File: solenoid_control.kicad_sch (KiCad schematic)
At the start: 37 parts, among them Q1 2N7002, Q10 DMG3406L, Q11 DMP3068L, Q12 DMG3406L, Q13 2N7002, Q14 DMP3068L, Q15 DMG3406L, Q16 DMP3068L, Q17 DMG3406L, Q19 2N7002, Q2 2N7002, Q3 DMP3068L, Q4 DMG3406L, Q5 DMP3068L, Q6 DMG3406L, Q7 2N7002, Q8 2N7002, Q9 DMP3068L

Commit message: Added connector for temperature sensor. Started to route board.
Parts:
- D14: value (none) -> BAT54S; footprint (none) -> Package_TO_SOT_SMD:SOT-23
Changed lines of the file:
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@@
       (effects (font (size 1.27 1.27)) (justify left))
     )
-    (property "Value" "" (id 1) (at 173.99 39.3699 90)
+    (property "Value" "BAT54S" (id 1) (at 173.99 39.3699 90)
       (effects (font (size 1.27 1.27)) (justify left))
     )
-    (property "Footprint" "" (id 2) (at 174.625 36.195 0)
+    (property "Footprint" "Package_TO_SOT_SMD:SOT-23" (id 2) (at 174.625 36.195 0)
       (effects (font (size 1.27 1.27)) (justify left) hide)
     )

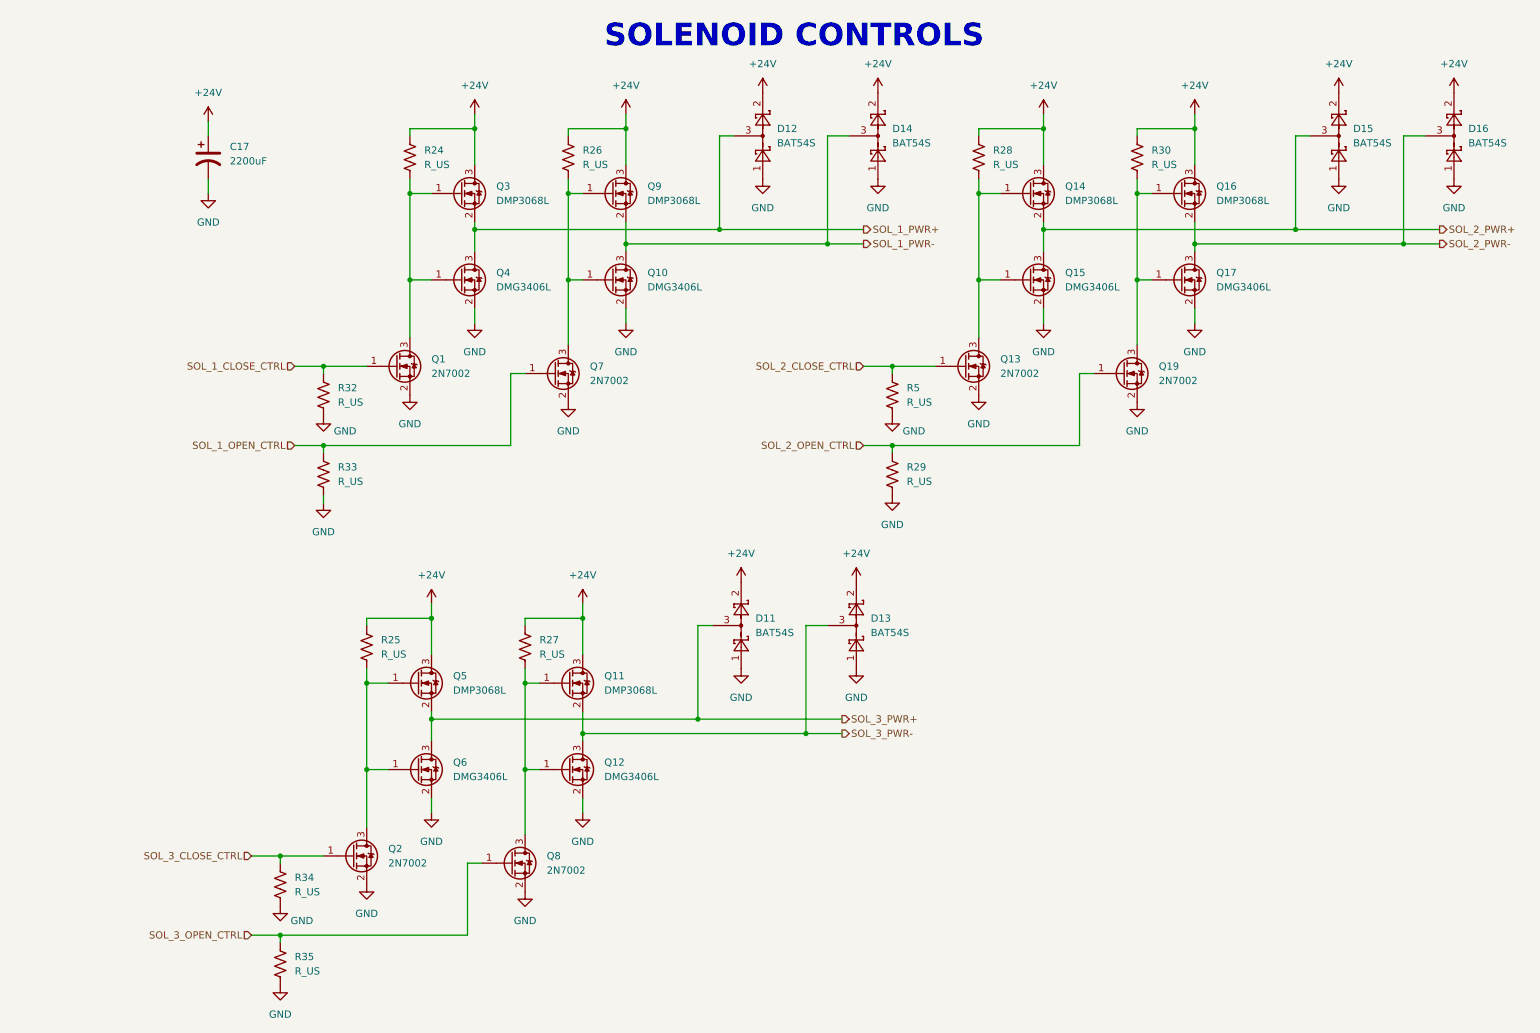
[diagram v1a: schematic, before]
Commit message: Added clamping diode for 24V net.
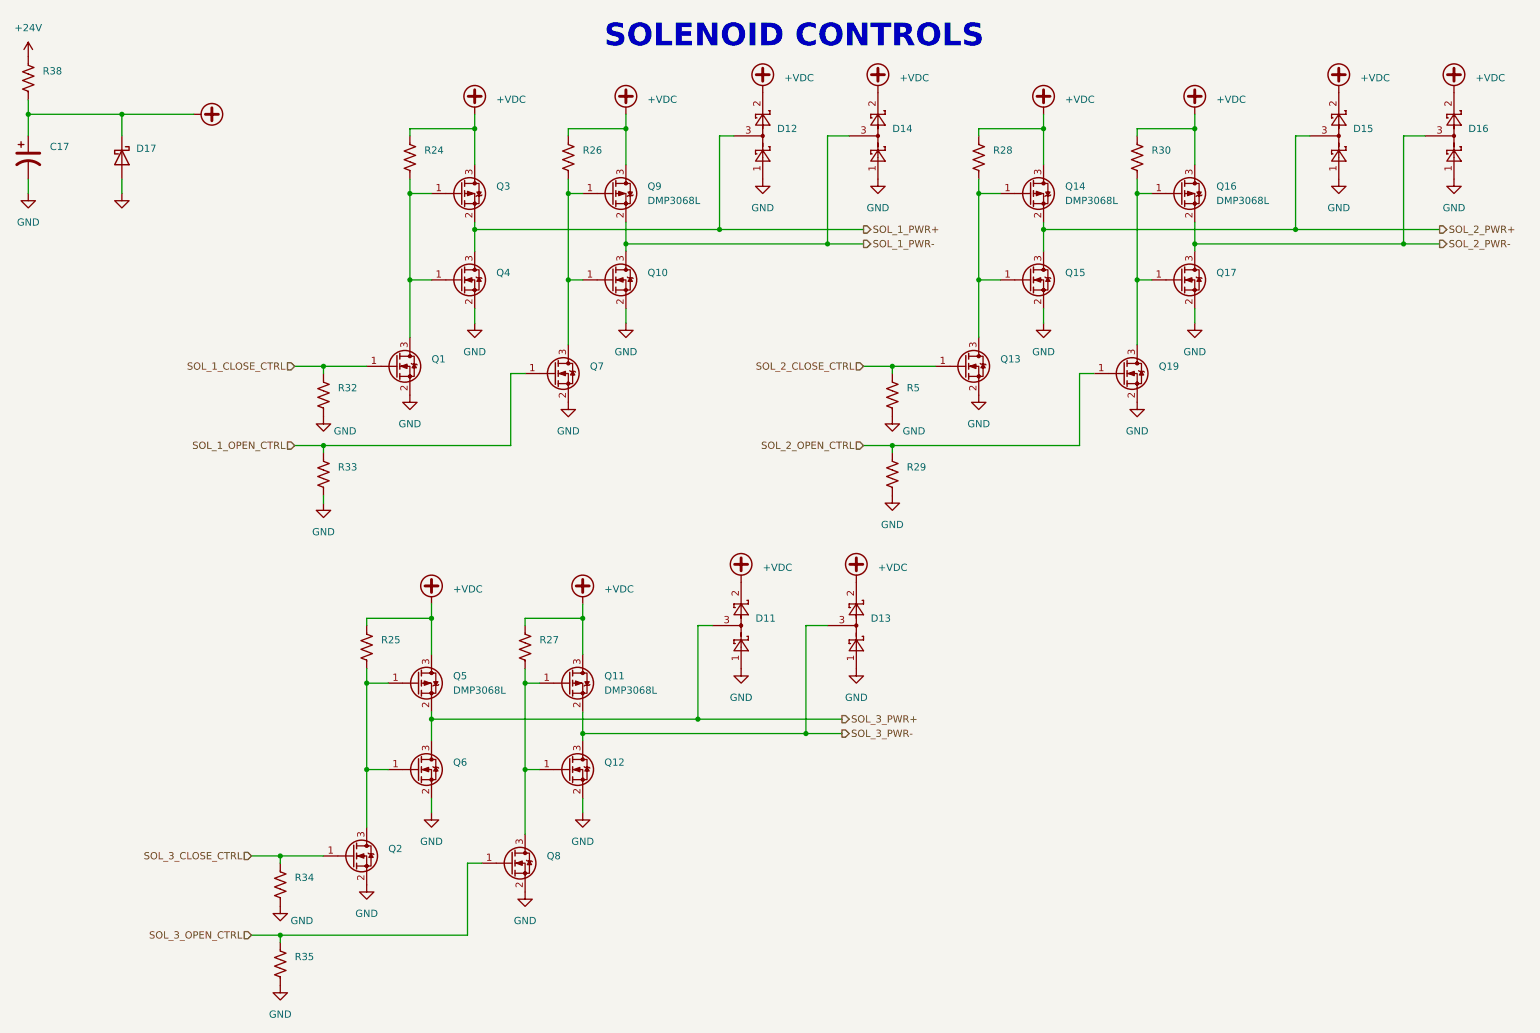
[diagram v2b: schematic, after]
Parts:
- removed Q11, Q14, Q16, Q3, Q5, Q9: DMP3068L, Package_TO_SOT_SMD:SOT-23, symbol Transistor_FET:2N7002
- added D17: (no value), symbol Diode:B140-E3
- added Q11, Q14, Q16, Q5, Q9: DMP3068L, Package_TO_SOT_SMD:SOT-23, symbol Transistor_FET:AO3401A
- added Q3: (no value), symbol Transistor_FET:AO3401A
- added R38: (no value), symbol Device:R_US
- C17: value 2200uF -> (none); footprint Capacitor_THT:CP_Radial_D16.0mm_P7.50mm -> (none)
- D11, D12, D13, D14, D15, D16: value BAT54S -> (none); footprint Package_TO_SOT_SMD:SOT-23 -> (none)
- Q1, Q13, Q19, Q2, Q7, Q8: value 2N7002 -> (none); footprint Package_TO_SOT_SMD:SOT-23 -> (none)
- Q10, Q12, Q15, Q17, Q4, Q6: value DMG3406L -> (none); footprint Package_TO_SOT_SMD:SOT-23 -> (none)
- R24, R25, R26, R27, R28, R29, R30, R32, R33, R34, R35, R5: value R_US -> (none); footprint Resistor_SMD:R_0805_2012Metric -> (none)
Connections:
- net +24V: now also R38.1; no longer C17.1, D11.2, D12.2, D13.2, D14.2, D15.2, D16.2, R24.1, R25.1, R26.1, R27.1, R28.1, R30.1
- net GND: now also D17.2 (A)
- net SOL_1_PWR+: now also Q3.2 (S)
- net SOL_1_PWR-: now also Q9.2 (S)
- net SOL_2_PWR+: now also Q14.2 (S)
- net SOL_2_PWR-: now also Q16.2 (S)
- net SOL_3_PWR+: now also Q5.2 (S)
- net SOL_3_PWR-: now also Q11.2 (S)
- net at Q12.1 (G), Q8.3 (D), R27.2: now also Q11.1 (G)
- net at Q17.1 (G), Q19.3 (D), R30.2: now also Q16.1 (G)
- net at Q10.1 (G), Q7.3 (D), R26.2: now also Q9.1 (G)
- net at Q1.3 (D), Q4.1 (G), R24.2: now also Q3.1 (G)
- net at Q2.3 (D), Q6.1 (G), R25.2: now also Q5.1 (G)
- net at Q13.3 (D), Q15.1 (G), R28.2: now also Q14.1 (G)
- new net +VDC: C17.1, D11.2, D12.2, D13.2, D14.2, D15.2, D16.2, D17.1 (K), Q11.3 (D), Q14.3 (D), Q16.3 (D), Q3.3 (D), Q5.3 (D), Q9.3 (D), R24.1, R25.1, R26.1, R27.1, R28.1, R30.1, R38.2
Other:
- moved on the sheet: C17

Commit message: Flipped top fets for solenoid controls so that the body diode was pointing the correction direction.
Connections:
- net +VDC: now also Q11.2 (S), Q14.2 (S), Q16.2 (S), Q3.2 (S), Q5.2 (S), Q9.2 (S); no longer Q11.3 (D), Q14.3 (D), Q16.3 (D), Q3.3 (D), Q5.3 (D), Q9.3 (D)
- net SOL_1_PWR+: now also Q3.3 (D); no longer Q3.2 (S)
- net SOL_1_PWR-: now also Q9.3 (D); no longer Q9.2 (S)
- net SOL_2_PWR+: now also Q14.3 (D); no longer Q14.2 (S)
- net SOL_2_PWR-: now also Q16.3 (D); no longer Q16.2 (S)
- net SOL_3_PWR+: now also Q5.3 (D); no longer Q5.2 (S)
- net SOL_3_PWR-: now also Q11.3 (D); no longer Q11.2 (S)
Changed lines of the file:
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@@
     (pin "3")
   )
-  (symbol (lib_id "Transistor_FET:AO3401A") (at 90.17 134.62 0) (unit 1)
+  (symbol (lib_id "Transistor_FET:AO3401A") (at 90.17 134.62 0) (mirror x) (unit 1)
     (in_bom yes) (on_board yes) (fields_autoplaced)
     (property "Reference" "Q5" (id 0) (at 96.52 133.3499 0)
@@
       (effects (font (size 1.27 1.27)) (justify left))
     )
-    (property "Footprint" "Package_TO_SOT_SMD:SOT-23" (id 2) (at 95.25 136.525 0)
+    (property "Footprint" "Package_TO_SOT_SMD:SOT-23" (id 2) (at 95.25 132.715 0)
       (effects (font (size 1.27 1.27) italic) (justify left) hide)
     )
@@
     (pin "1")
   )
-  (symbol (lib_id "Transistor_FET:AO3401A") (at 124.46 48.26 0) (unit 1)
+  (symbol (lib_id "Transistor_FET:AO3401A") (at 124.46 48.26 0) (mirror x) (unit 1)
     (in_bom yes) (on_board yes) (fields_autoplaced)
     (property "Reference" "Q9" (id 0) (at 130.81 46.9899 0)
@@
       (effects (font (size 1.27 1.27)) (justify left))
     )
-    (property "Footprint" "Package_TO_SOT_SMD:SOT-23" (id 2) (at 129.54 50.165 0)
+    (property "Footprint" "Package_TO_SOT_SMD:SOT-23" (id 2) (at 129.54 46.355 0)
       (effects (font (size 1.27 1.27) italic) (justify left) hide)
     )
@@
     (pin "3")
   )
-  (symbol (lib_id "Transistor_FET:AO3401A") (at 116.84 134.62 0) (unit 1)
+  (symbol (lib_id "Transistor_FET:AO3401A") (at 116.84 134.62 0) (mirror x) (unit 1)
     (in_bom yes) (on_board yes) (fields_autoplaced)
     (property "Reference" "Q11" (id 0) (at 123.19 133.3499 0)
@@
       (effects (font (size 1.27 1.27)) (justify left))
     )
-    (property "Footprint" "Package_TO_SOT_SMD:SOT-23" (id 2) (at 121.92 136.525 0)
+    (property "Footprint" "Package_TO_SOT_SMD:SOT-23" (id 2) (at 121.92 132.715 0)
       (effects (font (size 1.27 1.27) italic) (justify left) hide)
     )
@@
     (pin "1")
   )
-  (symbol (lib_id "Transistor_FET:AO3401A") (at 97.79 48.26 0) (unit 1)
+  (symbol (lib_id "Transistor_FET:AO3401A") (at 97.79 48.26 0) (mirror x) (unit 1)
     (in_bom yes) (on_board yes) (fields_autoplaced)
     (property "Reference" "Q3" (id 0) (at 104.14 46.9899 0)
@@
       (effects (font (size 1.27 1.27)) (justify left))
     )
-    (property "Footprint" "" (id 2) (at 102.87 50.165 0)
+    (property "Footprint" "" (id 2) (at 102.87 46.355 0)
       (effects (font (size 1.27 1.27) italic) (justify left) hide)
     )
@@
     (pin "1")
   )
-  (symbol (lib_id "Transistor_FET:AO3401A") (at 224.79 48.26 0) (unit 1)
+  (symbol (lib_id "Transistor_FET:AO3401A") (at 224.79 48.26 0) (mirror x) (unit 1)
     (in_bom yes) (on_board yes) (fields_autoplaced)
     (property "Reference" "Q16" (id 0) (at 231.14 46.9899 0)
@@
       (effects (font (size 1.27 1.27)) (justify left))
     )
-    (property "Footprint" "Package_TO_SOT_SMD:SOT-23" (id 2) (at 229.87 50.165 0)
+    (property "Footprint" "Package_TO_SOT_SMD:SOT-23" (id 2) (at 229.87 46.355 0)
       (effects (font (size 1.27 1.27) italic) (justify left) hide)
     )
@@
     (pin "1")
   )
-  (symbol (lib_id "Transistor_FET:AO3401A") (at 198.12 48.26 0) (unit 1)
+  (symbol (lib_id "Transistor_FET:AO3401A") (at 198.12 48.26 0) (mirror x) (unit 1)
     (in_bom yes) (on_board yes) (fields_autoplaced)
     (property "Reference" "Q14" (id 0) (at 204.47 46.9899 0)
@@
       (effects (font (size 1.27 1.27)) (justify left))
     )
-    (property "Footprint" "Package_TO_SOT_SMD:SOT-23" (id 2) (at 203.2 50.165 0)
-      (effects (font (size 1.27 1.27) italic) (justify left) hide)
-    )
+    (property "Footprint" "Package_TO_SOT_SMD:SOT-23" (id 2) (at 203.2 46.355 0)
+      (effects (font (size 1.27 1.27) italic) (justify left) hide)
+    )

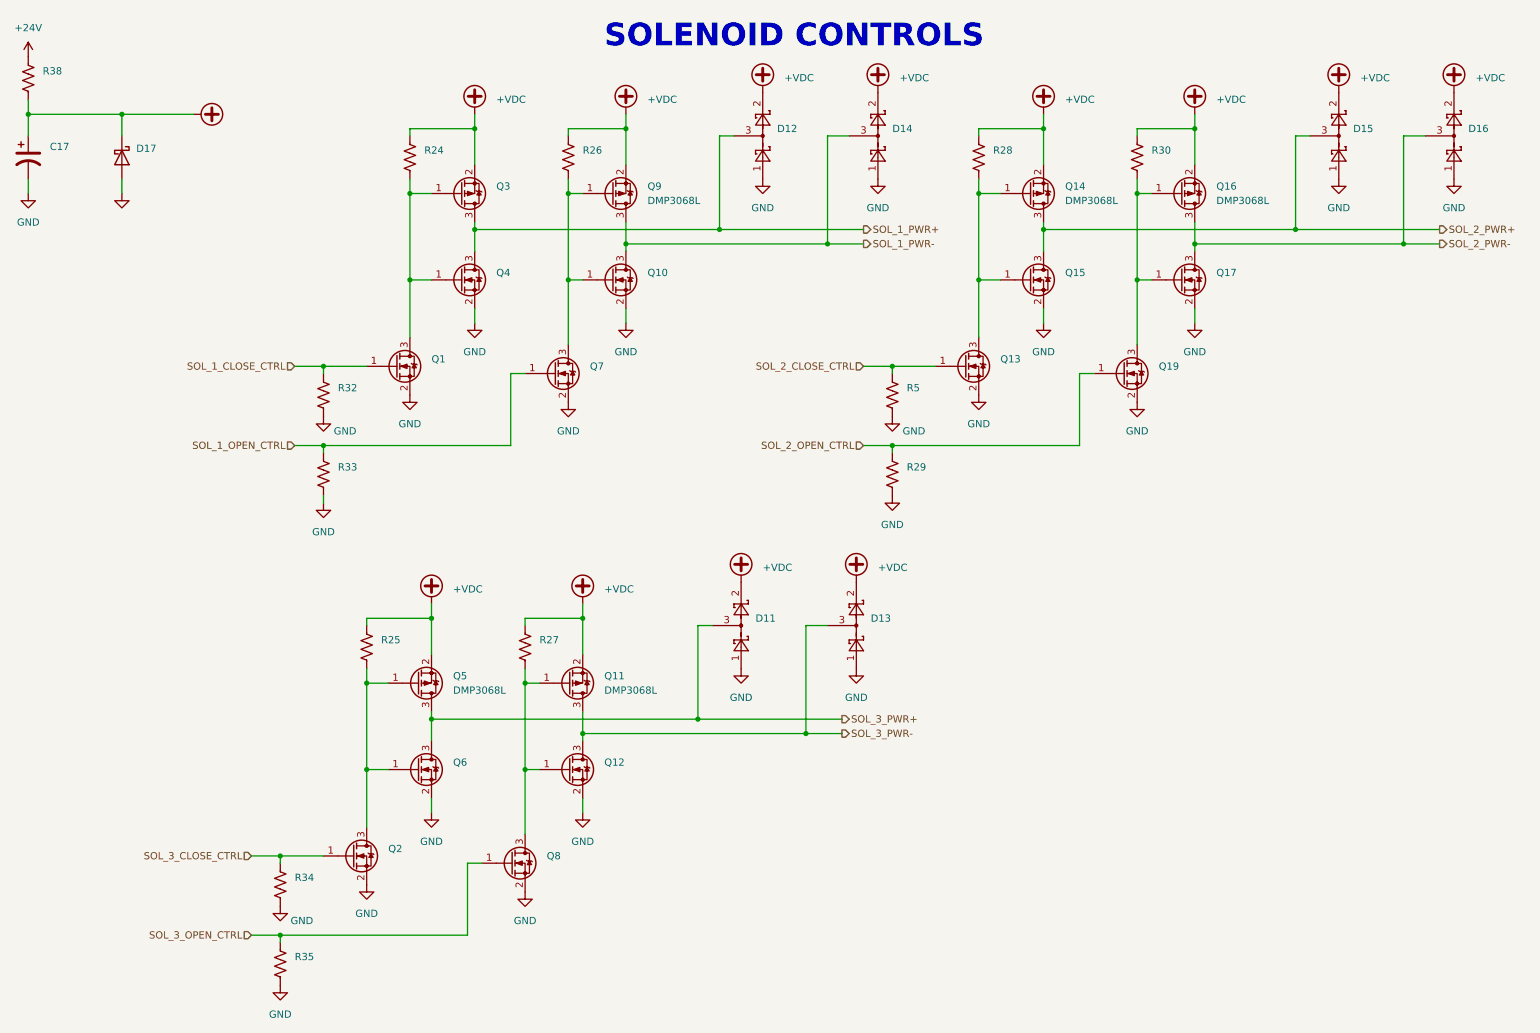
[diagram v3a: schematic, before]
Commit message: Finished initial layout.  Zero DRC errors/warnings.
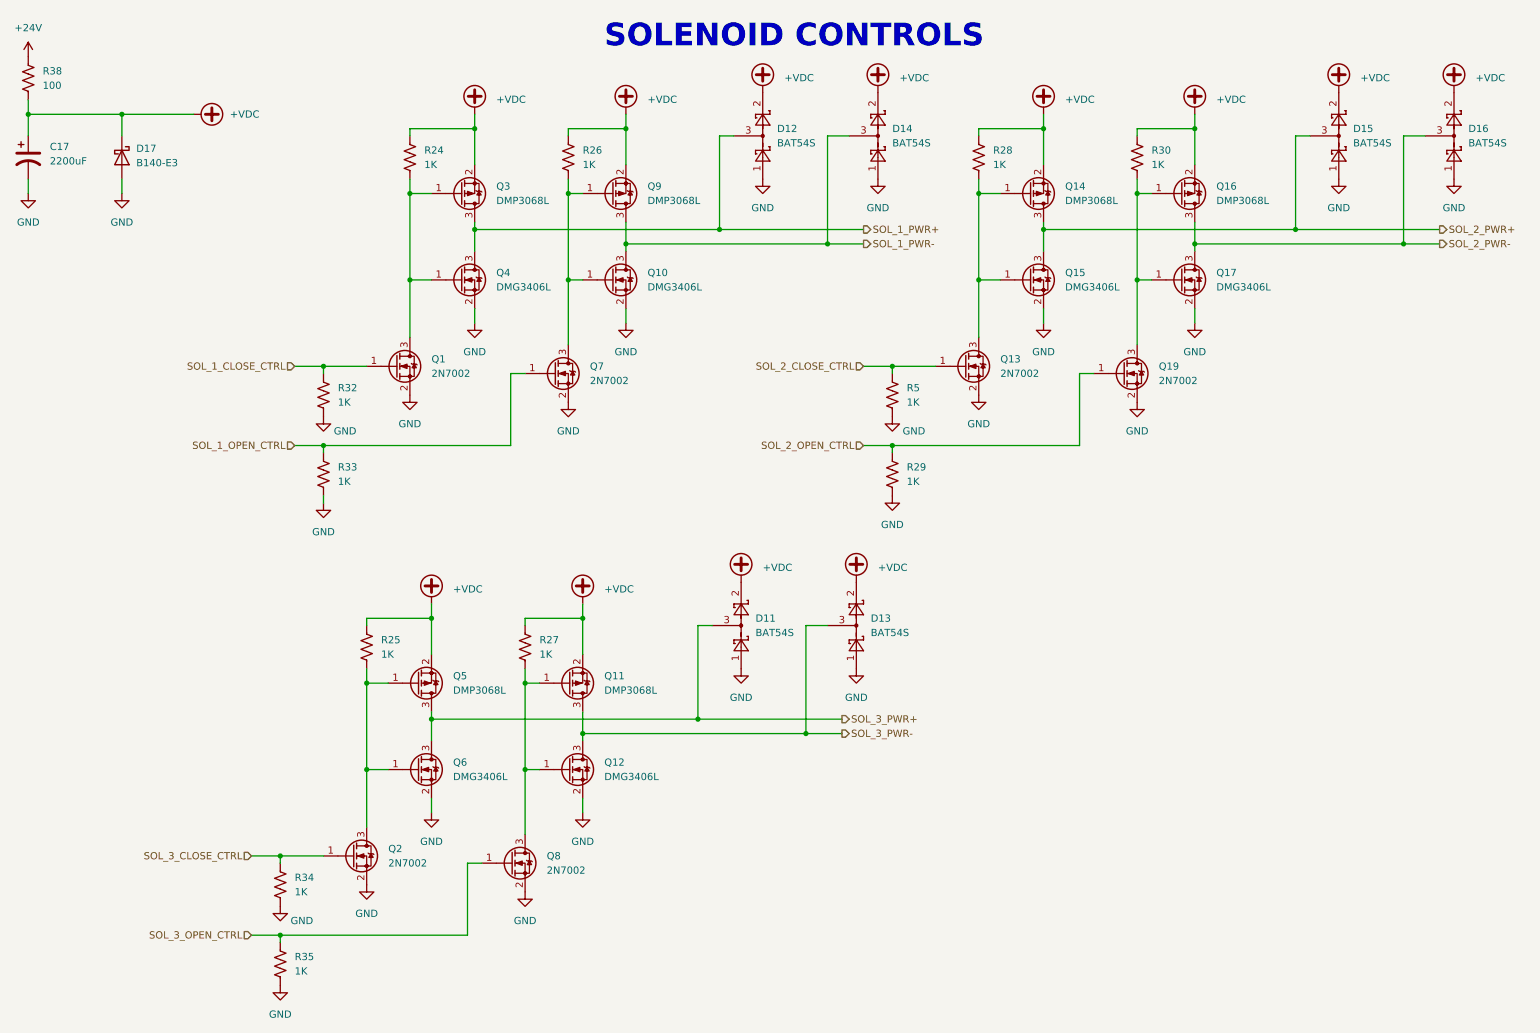
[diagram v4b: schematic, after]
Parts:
- C17: value (none) -> 2200uF; footprint (none) -> Capacitor_THT:CP_Radial_D16.0mm_P7.50mm
- D11, D12, D13, D14, D15, D16: value (none) -> BAT54S; footprint (none) -> Package_TO_SOT_SMD:SOT-23
- D17: value (none) -> B140-E3; footprint (none) -> Diode_SMD:D_SMA
- Q1, Q13, Q19, Q2, Q7, Q8: value (none) -> 2N7002; footprint (none) -> Package_TO_SOT_SMD:SOT-23
- Q10, Q12, Q15, Q17, Q4, Q6: value (none) -> DMG3406L; footprint (none) -> Package_TO_SOT_SMD:SOT-23
- Q3: value (none) -> DMP3068L; footprint (none) -> Package_TO_SOT_SMD:SOT-23
- R24, R25, R26, R27, R28, R29, R30, R32, R33, R34, R35, R5: value (none) -> 1K; footprint (none) -> Resistor_SMD:R_0805_2012Metric
- R38: value (none) -> 100; footprint (none) -> Resistor_SMD:R_2512_6332Metric
